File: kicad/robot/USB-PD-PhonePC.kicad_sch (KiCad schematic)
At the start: 44 parts, among them U11 MAX77958EWV+T, U15 ESD122DMYR, U16 fpf1048bucx, U17 TPS61253AYFFR

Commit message: Added stock counts to parts I have
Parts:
- U11: Stock (none) -> 25
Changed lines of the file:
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@@
+      (effects (font (size 1.27 1.27)) hide)
+    )
+    (property "Stock" "25" (id 6) (at 287.02 233.68 0)
       (effects (font (size 1.27 1.27)) hide)
     )

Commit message: Batch BOM edits adding manufactuer and part numbers only
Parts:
- L4: Manufacturer (none) -> Vishay
- R34, R35: Manufacturer (none) -> Stackpole Electronics; Part Number (none) -> RMCF0603JT2K20
- R36: Manufacturer (none) -> Stackpole Electronics; Part Number (none) -> RMCF0603JT200K
- R37, R39: Manufacturer (none) -> Stackpole Electronics; Part Number (none) -> RMCF0603FT649K
- R38, R40: Manufacturer (none) -> Stackpole Electronics; Part Number (none) -> RMCF0603JT120K
- U11: Manufacturer (none) -> Maxim
- U15: Manufacturer (none) -> Texas Instruments; manufacturer Texas Instruments -> (none)
- U16: Manufacturer (none) -> onsemi
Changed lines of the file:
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@@
   )
   (text "This should be kept low\nelse back currents can occur\nOnly test Forced PWM or Ultrasonic\nif you ensure no source present on\nVOUT"
-    (at 313.69 166.37 0)
+    (at 313.69 166.37 180)
     (effects (font (size 1.27 1.27)) (justify right bottom))
   )
@@
     )
     (property "Datasheet" "~" (id 3) (at 353.06 273.05 0)
+      (effects (font (size 1.27 1.27)) hide)
+    )
+    (property "Manufacturer" "Stackpole Electronics" (id 4) (at 353.06 273.05 0)
+      (effects (font (size 1.27 1.27)) hide)
+    )
+    (property "Part Number" "RMCF0603FT649K" (id 5) (at 353.06 273.05 0)
       (effects (font (size 1.27 1.27)) hide)
     )
@@
       (effects (font (size 1.27 1.27)) hide)
     )
+    (property "Manufacturer" "Stackpole Electronics" (id 4) (at 353.06 287.02 0)
+      (effects (font (size 1.27 1.27)) hide)
+    )
+    (property "Part Number" "RMCF0603JT120K" (id 5) (at 353.06 287.02 0)
+      (effects (font (size 1.27 1.27)) hide)
+    )
     (pin "1")
     (pin "2")
@@
     )
     (property "Datasheet" "~" (id 3) (at 334.01 229.87 0)
+      (effects (font (size 1.27 1.27)) hide)
+    )
+    (property "Manufacturer" "Stackpole Electronics" (id 4) (at 334.01 229.87 0)
+      (effects (font (size 1.27 1.27)) hide)
+    )
+    (property "Part Number" "RMCF0603JT200K" (id 5) (at 334.01 229.87 0)
       (effects (font (size 1.27 1.27)) hide)
     )
@@
       (effects (font (size 1.27 1.27)) hide)
     )
+    (property "Manufacturer" "Stackpole Electronics" (id 4) (at 339.09 287.02 0)
+      (effects (font (size 1.27 1.27)) hide)
+    )
+    (property "Part Number" "RMCF0603JT120K" (id 5) (at 339.09 287.02 0)
+      (effects (font (size 1.27 1.27)) hide)
+    )
     (pin "1")
     (pin "2")
@@
       (effects (font (size 1.27 1.27)) (justify left) hide)
     )
-    (property "manufacturer" "Texas Instruments" (id 21) (at 243.84 237.49 0)
+    (property "manufacturer" "" (id 21) (at 243.84 237.49 0)
       (effects (font (size 1.27 1.27)) (justify left) hide)
     )
@@
     )
     (property "Part Number" "ESD122DMYR" (id 32) (at 185.42 237.49 0)
+      (effects (font (size 1.27 1.27)) hide)
+    )
+    (property "Manufacturer" "Texas Instruments" (id 33) (at 185.42 237.49 0)
       (effects (font (size 1.27 1.27)) hide)
     )
@@
     )
     (property "Part Number" "fpf1048bucx" (id 4) (at 267.97 121.92 0)
+      (effects (font (size 1.27 1.27)) hide)
+    )
+    (property "Manufacturer" "onsemi" (id 5) (at 267.97 121.92 0)
       (effects (font (size 1.27 1.27)) hide)
     )
@@
       (effects (font (size 1.27 1.27)) hide)
     )
+    (property "Manufacturer" "Stackpole Electronics" (id 4) (at 339.09 273.05 0)
+      (effects (font (size 1.27 1.27)) hide)
+    )
+    (property "Part Number" "RMCF0603FT649K" (id 5) (at 339.09 273.05 0)
+      (effects (font (size 1.27 1.27)) hide)
+    )
     (pin "1")
     (pin "2")
@@
     )
     (property "Stock" "25" (id 6) (at 287.02 233.68 0)
+      (effects (font (size 1.27 1.27)) hide)
+    )
+    (property "Manufacturer" "Maxim" (id 7) (at 287.02 233.68 0)
       (effects (font (size 1.27 1.27)) hide)
     )
@@
       (effects (font (size 1.27 1.27)) hide)
     )
+    (property "Manufacturer" "Vishay" (id 6) (at 386.08 120.65 0)
+      (effects (font (size 1.27 1.27)) hide)
+    )
     (pin "1")
     (pin "2")
@@
     )
     (property "Datasheet" "~" (id 3) (at 312.42 187.96 0)
+      (effects (font (size 1.27 1.27)) hide)
+    )
+    (property "Manufacturer" "Stackpole Electronics" (id 4) (at 312.42 187.96 0)
+      (effects (font (size 1.27 1.27)) hide)
+    )
+    (property "Part Number" "RMCF0603JT2K20" (id 5) (at 312.42 187.96 0)
       (effects (font (size 1.27 1.27)) hide)
     )
@@
       (effects (font (size 1.27 1.27)) hide)
     )
+    (property "Manufacturer" "Stackpole Electronics" (id 4) (at 321.31 187.96 0)
+      (effects (font (size 1.27 1.27)) hide)
+    )
+    (property "Part Number" "RMCF0603JT2K20" (id 5) (at 321.31 187.96 0)
+      (effects (font (size 1.27 1.27)) hide)
+    )

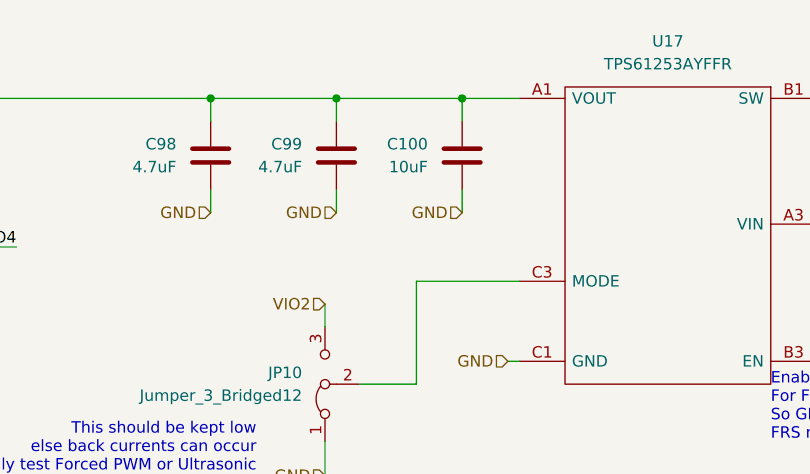
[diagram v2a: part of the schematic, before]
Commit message: bulk BOM edits. Mainly dealing with cap voltage ratings and part selection
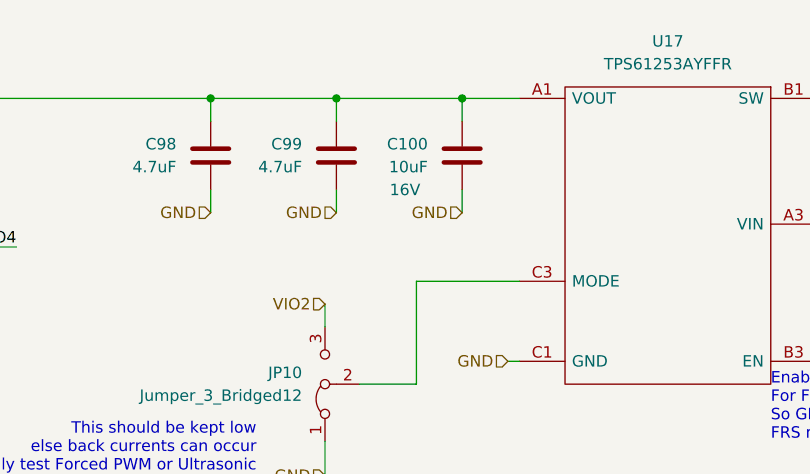
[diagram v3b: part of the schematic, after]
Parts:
- C100: Manufacturer (none) -> Samsung; Part Number (none) -> CL21A106KOQNNNG
- C101, C98, C99: Manufacturer (none) -> Samsung; Part Number (none) -> CL21A475KPFNNNE
- C45, C46: Manufacturer (none) -> Murata; Part Number (none) -> GRM1555C1H270JA01J
- C47, C48: Manufacturer (none) -> Samsung; Part Number (none) -> CL21B105KOFNNNE
- C49: Manufacturer (none) -> Samsung; Part Number (none) -> CL10A225KP8NNNC
- C50: Manufacturer (none) -> Taiyo Yuden; Part Number (none) -> GMK212BJ105KGHT
- C51, C52: Manufacturer (none) -> Samsung; Part Number (none) -> CL10A105KQ8NNNC
- C53, C54: Manufacturer (none) -> Samsung; Part Number (none) -> CL10A105KA8NNNC
- JP10, JP11, JP12: Manufacturer (none) -> Molex; Part Number (none) -> 22-28-4030
- JP2, JP3, JP4, JP5, JP6: Manufacturer (none) -> Adam Tech; Part Number (none) -> PH1-02-UA
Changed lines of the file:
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@@
     )
     (property "Description" "16V" (id 4) (at 226.06 163.83 0))
+    (property "Manufacturer" "Samsung" (id 5) (at 220.98 160.02 0)
+      (effects (font (size 1.27 1.27)) hide)
+    )
+    (property "Part Number" "CL21B105KOFNNNE" (id 6) (at 220.98 160.02 0)
+      (effects (font (size 1.27 1.27)) hide)
+    )
     (pin "1")
     (pin "2")
@@
       (effects (font (size 1.27 1.27)) hide)
     )
+    (property "Manufacturer" "Adam Tech" (id 5) (at 177.8 201.93 0)
+      (effects (font (size 1.27 1.27)) hide)
+    )
+    (property "Part Number" "PH1-02-UA" (id 6) (at 177.8 201.93 0)
+      (effects (font (size 1.27 1.27)) hide)
+    )
     (pin "1")
     (pin "2")
@@
     )
     (property "Description" "16V" (id 4) (at 224.79 262.89 0))
+    (property "Manufacturer" "Samsung" (id 5) (at 219.71 259.08 0)
+      (effects (font (size 1.27 1.27)) hide)
+    )
+    (property "Part Number" "CL21B105KOFNNNE" (id 6) (at 219.71 259.08 0)
+      (effects (font (size 1.27 1.27)) hide)
+    )
     (pin "1")
     (pin "2")
@@
       (effects (font (size 1.27 1.27)) hide)
     )
+    (property "Manufacturer" "Molex" (id 4) (at 439.42 255.27 0)
+      (effects (font (size 1.27 1.27)) hide)
+    )
+    (property "Part Number" "22-28-4030" (id 5) (at 439.42 255.27 0)
+      (effects (font (size 1.27 1.27)) hide)
+    )
     (pin "1")
     (pin "2")
@@
     )
     (property "Description" "10V" (id 4) (at 236.22 262.89 0))
+    (property "Manufacturer" "Samsung" (id 5) (at 231.14 259.08 0)
+      (effects (font (size 1.27 1.27)) hide)
+    )
+    (property "Part Number" "CL10A225KP8NNNC" (id 6) (at 231.14 259.08 0)
+      (effects (font (size 1.27 1.27)) hide)
+    )
     (pin "1")
     (pin "2")
@@
       (effects (font (size 1.27 1.27)) hide)
     )
+    (property "Manufacturer" "Adam Tech" (id 5) (at 194.31 153.67 0)
+      (effects (font (size 1.27 1.27)) hide)
+    )
+    (property "Part Number" "PH1-02-UA" (id 6) (at 194.31 153.67 0)
+      (effects (font (size 1.27 1.27)) hide)
+    )
     (pin "1")
     (pin "2")
@@
     )
     (property "Description" "6.3V" (id 4) (at 247.65 262.89 0))
+    (property "Manufacturer" "Samsung" (id 5) (at 242.57 259.08 0)
+      (effects (font (size 1.27 1.27)) hide)
+    )
+    (property "Part Number" "CL10A105KQ8NNNC" (id 6) (at 242.57 259.08 0)
+      (effects (font (size 1.27 1.27)) hide)
+    )
     (pin "1")
     (pin "2")
@@
       (effects (font (size 1.27 1.27)) hide)
     )
+    (property "Manufacturer" "Molex" (id 4) (at 439.42 274.32 0)
+      (effects (font (size 1.27 1.27)) hide)
+    )
+    (property "Part Number" "22-28-4030" (id 5) (at 439.42 274.32 0)
+      (effects (font (size 1.27 1.27)) hide)
+    )
     (pin "1")
     (pin "2")
@@
     )
     (property "Description" "50V" (id 4) (at 205.74 191.77 0))
+    (property "Manufacturer" "Murata" (id 5) (at 200.66 187.96 0)
+      (effects (font (size 1.27 1.27)) hide)
+    )
+    (property "Part Number" "GRM1555C1H270JA01J" (id 6) (at 200.66 187.96 0)
+      (effects (font (size 1.27 1.27)) hide)
+    )
     (pin "1")
     (pin "2")
@@
     )
     (property "Description" "" (id 4) (at 316.23 130.81 0))
+    (property "Manufacturer" "Samsung" (id 5) (at 322.58 127 0)
+      (effects (font (size 1.27 1.27)) hide)
+    )
+    (property "Part Number" "CL21A475KPFNNNE" (id 6) (at 322.58 127 0)
+      (effects (font (size 1.27 1.27)) hide)
+    )
     (pin "1")
     (pin "2")
@@
     )
     (property "Description" "6.3V" (id 4) (at 259.08 262.89 0))
+    (property "Manufacturer" "Samsung" (id 5) (at 252.73 259.08 0)
+      (effects (font (size 1.27 1.27)) hide)
+    )
+    (property "Part Number" "CL10A105KQ8NNNC" (id 6) (at 252.73 259.08 0)
+      (effects (font (size 1.27 1.27)) hide)
+    )
     (pin "1")
     (pin "2")
@@
     )
     (property "Description" "2.54mm male header with jumper attached" (id 4) (at 361.95 246.38 0)
+      (effects (font (size 1.27 1.27)) hide)
+    )
+    (property "Manufacturer" "Adam Tech" (id 5) (at 361.95 246.38 0)
+      (effects (font (size 1.27 1.27)) hide)
+    )
+    (property "Part Number" "PH1-02-UA" (id 6) (at 361.95 246.38 0)
       (effects (font (size 1.27 1.27)) hide)
     )
@@
     )
     (property "Description" "50V" (id 4) (at 218.44 187.96 0))
+    (property "Manufacturer" "Murata" (id 5) (at 213.36 184.15 0)
+      (effects (font (size 1.27 1.27)) hide)
+    )
+    (property "Part Number" "GRM1555C1H270JA01J" (id 6) (at 213.36 184.15 0)
+      (effects (font (size 1.27 1.27)) hide)
+    )
     (pin "1")
     (pin "2")
@@
     )
     (property "Description" "35V" (id 4) (at 240.03 130.81 0))
+    (property "Manufacturer" "Taiyo Yuden" (id 5) (at 233.68 127 0)
+      (effects (font (size 1.27 1.27)) hide)
+    )
+    (property "Part Number" "GMK212BJ105KGHT" (id 6) (at 233.68 127 0)
+      (effects (font (size 1.27 1.27)) hide)
+    )
     (pin "1")
     (pin "2")
@@
     )
     (property "Datasheet" "~" (id 3) (at 321.31 152.4 0)
+      (effects (font (size 1.27 1.27)) hide)
+    )
+    (property "Manufacturer" "Molex" (id 4) (at 321.31 152.4 0)
+      (effects (font (size 1.27 1.27)) hide)
+    )
+    (property "Part Number" "22-28-4030" (id 5) (at 321.31 152.4 0)
       (effects (font (size 1.27 1.27)) hide)
     )
@@
       (effects (font (size 1.27 1.27)) hide)
     )
+    (property "Manufacturer" "Adam Tech" (id 5) (at 378.46 210.82 0)
+      (effects (font (size 1.27 1.27)) hide)
+    )
+    (property "Part Number" "PH1-02-UA" (id 6) (at 378.46 210.82 0)
+      (effects (font (size 1.27 1.27)) hide)
+    )
     (pin "1")
     (pin "2")
@@
     )
     (property "Description" "" (id 4) (at 403.86 130.81 0))
+    (property "Manufacturer" "Samsung" (id 5) (at 410.21 127 0)
+      (effects (font (size 1.27 1.27)) hide)
+    )
+    (property "Part Number" "CL21A475KPFNNNE" (id 6) (at 410.21 127 0)
+      (effects (font (size 1.27 1.27)) hide)
+    )
     (pin "1")
     (pin "2")
@@
       (effects (font (size 1.27 1.27)) hide)
     )
-    (property "Description" "" (id 4) (at 330.2 130.81 0))
+    (property "Description" "16V" (id 4) (at 330.2 130.81 0))
+    (property "Manufacturer" "Samsung" (id 5) (at 336.55 127 0)
+      (effects (font (size 1.27 1.27)) hide)
+    )
+    (property "Part Number" "CL21A106KOQNNNG" (id 6) (at 336.55 127 0)
+      (effects (font (size 1.27 1.27)) hide)
+    )
     (pin "1")
     (pin "2")
@@
     )
     (property "Description" "16V" (id 4) (at 337.82 254 0))
+    (property "Manufacturer" "Samsung" (id 5) (at 331.47 250.19 0)
+      (effects (font (size 1.27 1.27)) hide)
+    )
+    (property "Part Number" "CL10A105KA8NNNC" (id 6) (at 331.47 250.19 0)
+      (effects (font (size 1.27 1.27)) hide)
+    )
     (pin "1")
     (pin "2")
@@
     )
     (property "Description" "16V" (id 4) (at 354.33 218.44 0))
+    (property "Manufacturer" "Samsung" (id 5) (at 347.98 214.63 0)
+      (effects (font (size 1.27 1.27)) hide)
+    )
+    (property "Part Number" "CL10A105KA8NNNC" (id 6) (at 347.98 214.63 0)
+      (effects (font (size 1.27 1.27)) hide)
+    )
     (pin "1")
     (pin "2")
@@
     )
     (property "Description" "" (id 4) (at 302.26 130.81 0))
+    (property "Manufacturer" "Samsung" (id 5) (at 308.61 127 0)
+      (effects (font (size 1.27 1.27)) hide)
+    )
+    (property "Part Number" "CL21A475KPFNNNE" (id 6) (at 308.61 127 0)
+      (effects (font (size 1.27 1.27)) hide)
+    )
     (pin "1")
     (pin "2")
@@
       (effects (font (size 1.27 1.27)) hide)
     )
+    (property "Manufacturer" "Adam Tech" (id 5) (at 218.44 120.65 0)
+      (effects (font (size 1.27 1.27)) hide)
+    )
+    (property "Part Number" "PH1-02-UA" (id 6) (at 218.44 120.65 0)
+      (effects (font (size 1.27 1.27)) hide)
+    )

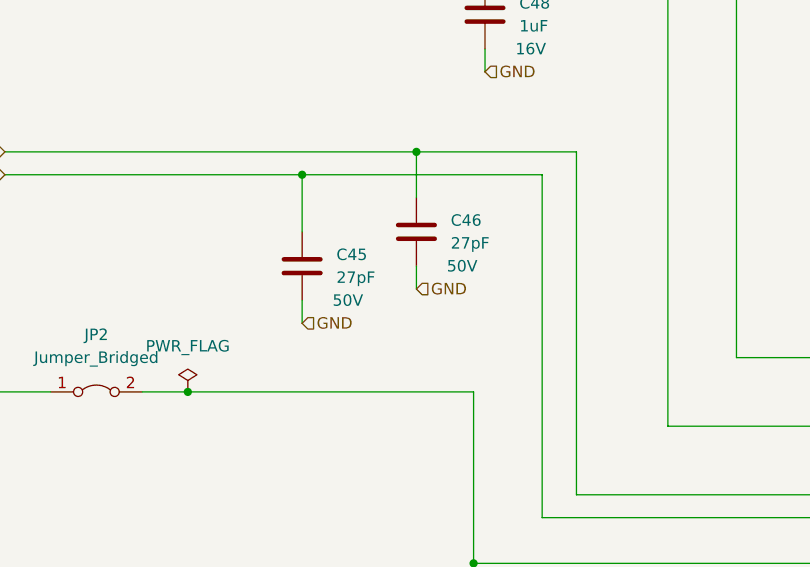
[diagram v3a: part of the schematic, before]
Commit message: Updating bulk caps on USB VBUS
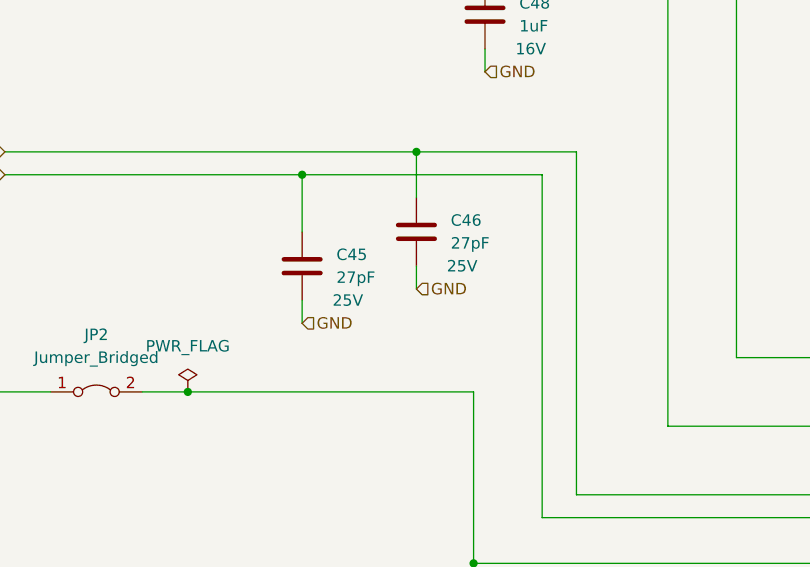
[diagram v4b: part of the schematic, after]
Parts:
- C45, C46: Manufacturer Murata -> (none); Part Number GRM1555C1H270JA01J -> (none)
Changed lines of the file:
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@@
       (effects (font (size 1.27 1.27)) hide)
     )
-    (property "Description" "50V" (id 4) (at 205.74 191.77 0))
-    (property "Manufacturer" "Murata" (id 5) (at 200.66 187.96 0)
-      (effects (font (size 1.27 1.27)) hide)
-    )
-    (property "Part Number" "GRM1555C1H270JA01J" (id 6) (at 200.66 187.96 0)
-      (effects (font (size 1.27 1.27)) hide)
-    )
+    (property "Description" "25V" (id 4) (at 205.74 191.77 0))
     (pin "1")
     (pin "2")
@@
       (effects (font (size 1.27 1.27)) hide)
     )
-    (property "Description" "50V" (id 4) (at 218.44 187.96 0))
-    (property "Manufacturer" "Murata" (id 5) (at 213.36 184.15 0)
-      (effects (font (size 1.27 1.27)) hide)
-    )
-    (property "Part Number" "GRM1555C1H270JA01J" (id 6) (at 213.36 184.15 0)
-      (effects (font (size 1.27 1.27)) hide)
-    )
-    (pin "1")
-    (pin "2")
+    (property "Description" "25V" (id 4) (at 218.44 187.96 0))
+    (pin "1")
+    (pin "2")
